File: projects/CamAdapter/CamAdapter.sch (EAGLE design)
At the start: 2 parts

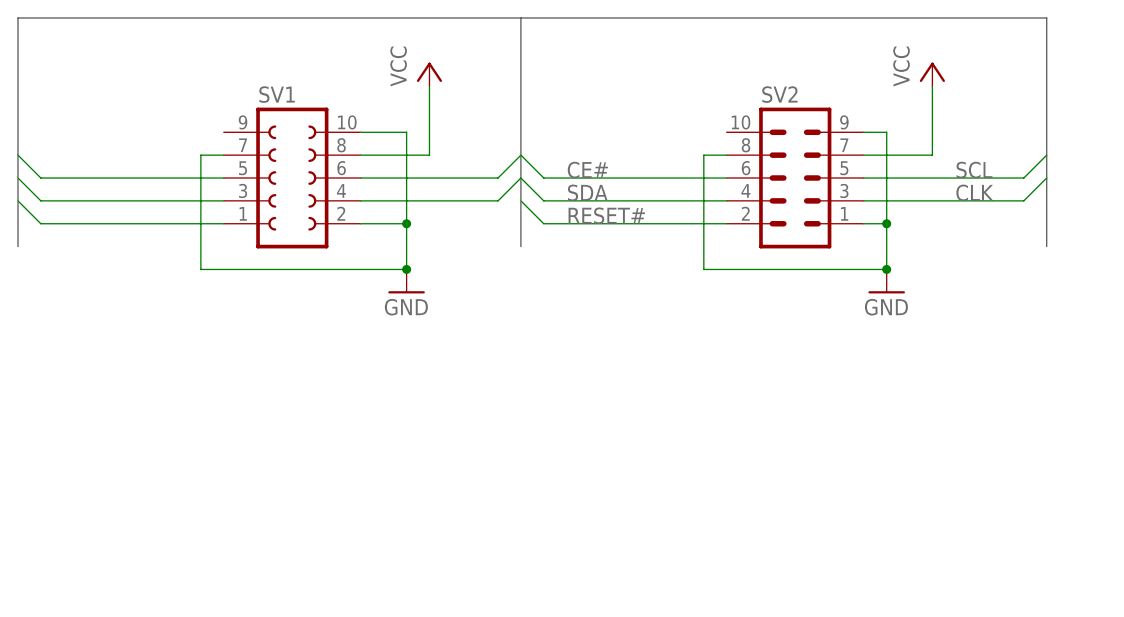
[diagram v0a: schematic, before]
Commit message: Updated CamAdapter + Board
* Added 25 MHz resonator to adapter board
* Removed 25 MHz CLK signal from PCB connector
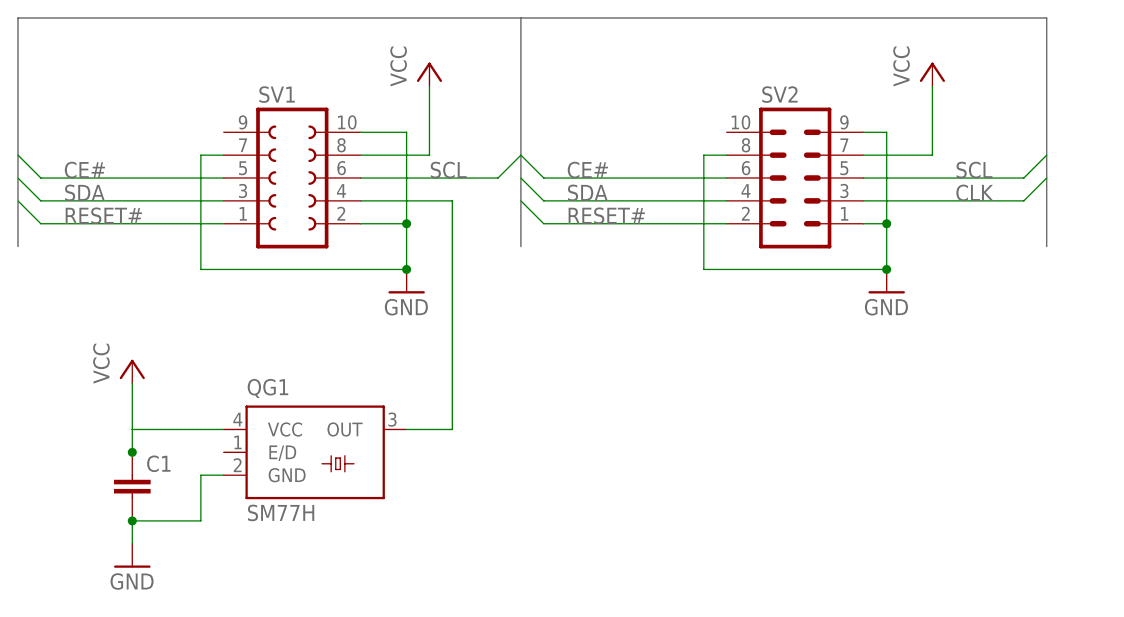
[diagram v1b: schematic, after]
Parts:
- added C1: (no value), resistor:C-EUC0805
- added QG1: SM77H, crystal:SM77H
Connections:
- new net N$1: QG1.OUT, SV1.4
- net CLK: no longer SV1.4
- net GND: now also C1.2, QG1.GND
- net VCC: now also C1.1, QG1.VCC
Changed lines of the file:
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@@
 <grid distance="0.1" unitdist="inch" unit="inch" style="lines" multiple="1" display="no" altdistance="0.01" altunitdist="inch" altunit="inch"/>
 <layers>
-<layer number="1" name="Top" color="4" fill="1" visible="no" active="no"/>
-<layer number="16" name="Bottom" color="1" fill="1" visible="no" active="no"/>
-<layer number="17" name="Pads" color="2" fill="1" visible="no" active="no"/>
-<layer number="18" name="Vias" color="2" fill="1" visible="no" active="no"/>
-<layer number="19" name="Unrouted" color="6" fill="1" visible="no" active="no"/>
-<layer number="20" name="Dimension" color="15" fill="1" visible="no" active="no"/>
-<layer number="21" name="tPlace" color="7" fill="1" visible="no" active="no"/>
-<layer number="22" name="bPlace" color="7" fill="1" visible="no" active="no"/>
-<layer number="23" name="tOrigins" color="15" fill="1" visible="no" active="no"/>
-<layer number="24" name="bOrigins" color="15" fill="1" visible="no" active="no"/>
-<layer number="25" name="tNames" color="7" fill="1" visible="no" active="no"/>
-<layer number="26" name="bNames" color="7" fill="1" visible="no" active="no"/>
-<layer number="27" name="tValues" color="7" fill="1" visible="no" active="no"/>
-<layer number="28" name="bValues" color="7" fill="1" visible="no" active="no"/>
+<layer number="1" name="Top" color="4" fill="1" visible="yes" active="no"/>
+<layer number="16" name="Bottom" color="1" fill="1" visible="yes" active="no"/>
+<layer number="17" name="Pads" color="2" fill="1" visible="yes" active="no"/>
+<layer number="18" name="Vias" color="2" fill="1" visible="yes" active="no"/>
+<layer number="19" name="Unrouted" color="6" fill="1" visible="yes" active="no"/>
+<layer number="20" name="Dimension" color="15" fill="1" visible="yes" active="no"/>
+<layer number="21" name="tPlace" color="7" fill="1" visible="yes" active="no"/>
+<layer number="22" name="bPlace" color="7" fill="1" visible="yes" active="no"/>
+<layer number="23" name="tOrigins" color="15" fill="1" visible="yes" active="no"/>
+<layer number="24" name="bOrigins" color="15" fill="1" visible="yes" active="no"/>
+<layer number="25" name="tNames" color="7" fill="1" visible="yes" active="no"/>
+<layer number="26" name="bNames" color="7" fill="1" visible="yes" active="no"/>
+<layer number="27" name="tValues" color="7" fill="1" visible="yes" active="no"/>
+<layer number="28" name="bValues" color="7" fill="1" visible="yes" active="no"/>
 <layer number="29" name="tStop" color="7" fill="3" visible="no" active="no"/>
 <layer number="30" name="bStop" color="7" fill="6" visible="no" active="no"/>
@@
 <layer number="35" name="tGlue" color="7" fill="4" visible="no" active="no"/>
 <layer number="36" name="bGlue" color="7" fill="5" visible="no" active="no"/>
-<layer number="37" name="tTest" color="7" fill="1" visible="no" active="no"/>
-<layer number="38" name="bTest" color="7" fill="1" visible="no" active="no"/>
+<layer number="37" name="tTest" color="7" fill="1" visible="yes" active="no"/>
+<layer number="38" name="bTest" color="7" fill="1" visible="yes" active="no"/>
 <layer number="39" name="tKeepout" color="4" fill="11" visible="no" active="no"/>
 <layer number="40" name="bKeepout" color="1" fill="11" visible="no" active="no"/>
@@
 <layer number="44" name="Drills" color="7" fill="1" visible="no" active="no"/>
 <layer number="45" name="Holes" color="7" fill="1" visible="no" active="no"/>
-<layer number="46" name="Milling" color="3" fill="1" visible="no" active="no"/>
-<layer number="47" name="Measures" color="7" fill="1" visible="no" active="no"/>
-<layer number="48" name="Document" color="7" fill="1" visible="no" active="no"/>
-<layer number="49" name="Reference" color="7" fill="1" visible="no" active="no"/>
-<layer number="51" name="tDocu" color="7" fill="1" visible="no" active="no"/>
-<layer number="52" name="bDocu" color="7" fill="1" visible="no" active="no"/>
+<layer number="46" name="Milling" color="3" fill="1" visible="yes" active="no"/>
+<layer number="47" name="Measures" color="7" fill="1" visible="yes" active="no"/>
+<layer number="48" name="Document" color="7" fill="1" visible="yes" active="no"/>
+<layer number="49" name="Reference" color="7" fill="1" visible="yes" active="no"/>
+<layer number="51" name="tDocu" color="7" fill="1" visible="yes" active="no"/>
+<layer number="52" name="bDocu" color="7" fill="1" visible="yes" active="no"/>
 <layer number="91" name="Nets" color="2" fill="1" visible="yes" active="yes"/>
 <layer number="92" name="Busses" color="1" fill="1" visible="yes" active="yes"/>
@@
 <part name="P+1" library="supply1" deviceset="VCC" device=""/>
 <part name="P+2" library="supply1" deviceset="VCC" device=""/>
+<part name="QG1" library="crystal" deviceset="SM77H" device=""/>
+<part name="C1" library="resistor" deviceset="C-EU" device="C0805"/>
+<part name="P+3" library="supply1" deviceset="VCC" device=""/>
+<part name="GND3" library="supply1" deviceset="GND" device=""/>
 </parts>
 <sheets>
@@
 <instance part="P+1" gate="VCC" x="93.98" y="127"/>
 <instance part="P+2" gate="VCC" x="149.86" y="127"/>
+<instance part="QG1" gate="G$1" x="81.28" y="83.82"/>
+<instance part="C1" gate="G$1" x="60.96" y="81.28"/>
+<instance part="P+3" gate="VCC" x="60.96" y="93.98"/>
+<instance part="GND3" gate="1" x="60.96" y="71.12"/>
 </instances>
 <busses>
@@
 <wire x1="71.12" y1="109.22" x2="50.8" y2="109.22" width="0.1524" layer="91"/>
 <wire x1="50.8" y1="109.22" x2="48.26" y2="111.76" width="0.1524" layer="91"/>
+<label x="53.34" y="109.22" size="1.778" layer="95"/>
 </segment>
 </net>
@@
 <label x="152.4" y="111.76" size="1.778" layer="95"/>
 </segment>
-<segment>
-<pinref part="SV1" gate="G$1" pin="4"/>
-<wire x1="86.36" y1="111.76" x2="101.6" y2="111.76" width="0.1524" layer="91"/>
-<wire x1="101.6" y1="111.76" x2="104.14" y2="114.3" width="0.1524" layer="91"/>
-</segment>
 </net>
 <net name="SDA" class="0">
@@
 <wire x1="71.12" y1="111.76" x2="50.8" y2="111.76" width="0.1524" layer="91"/>
 <wire x1="50.8" y1="111.76" x2="48.26" y2="114.3" width="0.1524" layer="91"/>
+<label x="53.34" y="111.76" size="1.778" layer="95"/>
 </segment>
 </net>
@@
 <wire x1="86.36" y1="114.3" x2="101.6" y2="114.3" width="0.1524" layer="91"/>
 <wire x1="101.6" y1="114.3" x2="104.14" y2="116.84" width="0.1524" layer="91"/>
+<label x="93.98" y="114.3" size="1.778" layer="95"/>
 </segment>
 </net>
@@
 <wire x1="71.12" y1="114.3" x2="50.8" y2="114.3" width="0.1524" layer="91"/>
 <wire x1="50.8" y1="114.3" x2="48.26" y2="116.84" width="0.1524" layer="91"/>
+<label x="53.34" y="114.3" size="1.778" layer="95"/>
 </segment>
 </net>
@@
 <junction x="91.44" y="109.22"/>
 </segment>
+<segment>
+<pinref part="QG1" gate="G$1" pin="GND"/>
+<wire x1="71.12" y1="81.28" x2="68.58" y2="81.28" width="0.1524" layer="91"/>
+<wire x1="68.58" y1="81.28" x2="68.58" y2="76.2" width="0.1524" layer="91"/>
+<pinref part="C1" gate="G$1" pin="2"/>
+<wire x1="68.58" y1="76.2" x2="60.96" y2="76.2" width="0.1524" layer="91"/>
+<pinref part="GND3" gate="1" pin="GND"/>
+<wire x1="60.96" y1="76.2" x2="60.96" y2="73.66" width="0.1524" layer="91"/>
+<junction x="60.96" y="76.2"/>
+</segment>
 </net>
 <net name="VCC" class="0">
@@
 <wire x1="93.98" y1="116.84" x2="93.98" y2="124.46" width="0.1524" layer="91"/>
 </segment>
-</net>
+<segment>
+<pinref part="QG1" gate="G$1" pin="VCC"/>
+<pinref part="P+3" gate="VCC" pin="VCC"/>
+<wire x1="71.12" y1="86.36" x2="60.96" y2="86.36" width="0.1524" layer="91"/>
+<wire x1="60.96" y1="86.36" x2="60.96" y2="91.44" width="0.1524" layer="91"/>
+<pinref part="C1" gate="G$1" pin="1"/>
+<wire x1="60.96" y1="83.82" x2="60.96" y2="86.36" width="0.1524" layer="91"/>
+<junction x="60.96" y="83.82"/>
+</segment>
+</net>
+<net name="N$1" class="0">
+<segment>
+<pinref part="QG1" gate="G$1" pin="OUT"/>
+<wire x1="91.44" y1="86.36" x2="96.52" y2="86.36" width="0.1524" layer="91"/>
+<wire x1="96.52" y1="86.36" x2="96.52" y2="111.76" width="0.1524" layer="91"/>
+<pinref part="SV1" gate="G$1" pin="4"/>
+<wire x1="96.52" y1="111.76" x2="86.36" y2="111.76" width="0.1524" layer="91"/>
+</segment>
+</net>

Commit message: Rev 2.0 RC
* TODO: Check CamAdapter.brd quarz oscillator package
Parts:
- C1: value (none) -> 100n
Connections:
- net VCC: now also QG1.E/D
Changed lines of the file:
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@@
 <part name="P+2" library="supply1" deviceset="VCC" device=""/>
 <part name="QG1" library="crystal" deviceset="SM77H" device=""/>
-<part name="C1" library="resistor" deviceset="C-EU" device="C0805"/>
+<part name="C1" library="resistor" deviceset="C-EU" device="C0805" value="100n"/>
 <part name="P+3" library="supply1" deviceset="VCC" device=""/>
 <part name="GND3" library="supply1" deviceset="GND" device=""/>
@@
 <wire x1="60.96" y1="83.82" x2="60.96" y2="86.36" width="0.1524" layer="91"/>
 <junction x="60.96" y="83.82"/>
+<pinref part="QG1" gate="G$1" pin="E/D"/>
+<wire x1="71.12" y1="83.82" x2="60.96" y2="83.82" width="0.1524" layer="91"/>
 </segment>
 </net>

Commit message: Enhaced space between signal trace and female pin header
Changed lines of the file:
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@@
 <grid distance="0.1" unitdist="inch" unit="inch" style="lines" multiple="1" display="no" altdistance="0.01" altunitdist="inch" altunit="inch"/>
 <layers>
-<layer number="1" name="Top" color="4" fill="1" visible="yes" active="no"/>
-<layer number="16" name="Bottom" color="1" fill="1" visible="yes" active="no"/>
-<layer number="17" name="Pads" color="2" fill="1" visible="yes" active="no"/>
-<layer number="18" name="Vias" color="2" fill="1" visible="yes" active="no"/>
-<layer number="19" name="Unrouted" color="6" fill="1" visible="yes" active="no"/>
-<layer number="20" name="Dimension" color="15" fill="1" visible="yes" active="no"/>
-<layer number="21" name="tPlace" color="7" fill="1" visible="yes" active="no"/>
-<layer number="22" name="bPlace" color="7" fill="1" visible="yes" active="no"/>
-<layer number="23" name="tOrigins" color="15" fill="1" visible="yes" active="no"/>
-<layer number="24" name="bOrigins" color="15" fill="1" visible="yes" active="no"/>
-<layer number="25" name="tNames" color="7" fill="1" visible="yes" active="no"/>
-<layer number="26" name="bNames" color="7" fill="1" visible="yes" active="no"/>
-<layer number="27" name="tValues" color="7" fill="1" visible="yes" active="no"/>
-<layer number="28" name="bValues" color="7" fill="1" visible="yes" active="no"/>
+<layer number="1" name="Top" color="4" fill="1" visible="no" active="no"/>
+<layer number="16" name="Bottom" color="1" fill="1" visible="no" active="no"/>
+<layer number="17" name="Pads" color="2" fill="1" visible="no" active="no"/>
+<layer number="18" name="Vias" color="2" fill="1" visible="no" active="no"/>
+<layer number="19" name="Unrouted" color="6" fill="1" visible="no" active="no"/>
+<layer number="20" name="Dimension" color="15" fill="1" visible="no" active="no"/>
+<layer number="21" name="tPlace" color="7" fill="1" visible="no" active="no"/>
+<layer number="22" name="bPlace" color="7" fill="1" visible="no" active="no"/>
+<layer number="23" name="tOrigins" color="15" fill="1" visible="no" active="no"/>
+<layer number="24" name="bOrigins" color="15" fill="1" visible="no" active="no"/>
+<layer number="25" name="tNames" color="7" fill="1" visible="no" active="no"/>
+<layer number="26" name="bNames" color="7" fill="1" visible="no" active="no"/>
+<layer number="27" name="tValues" color="7" fill="1" visible="no" active="no"/>
+<layer number="28" name="bValues" color="7" fill="1" visible="no" active="no"/>
 <layer number="29" name="tStop" color="7" fill="3" visible="no" active="no"/>
 <layer number="30" name="bStop" color="7" fill="6" visible="no" active="no"/>
@@
 <layer number="35" name="tGlue" color="7" fill="4" visible="no" active="no"/>
 <layer number="36" name="bGlue" color="7" fill="5" visible="no" active="no"/>
-<layer number="37" name="tTest" color="7" fill="1" visible="yes" active="no"/>
-<layer number="38" name="bTest" color="7" fill="1" visible="yes" active="no"/>
+<layer number="37" name="tTest" color="7" fill="1" visible="no" active="no"/>
+<layer number="38" name="bTest" color="7" fill="1" visible="no" active="no"/>
 <layer number="39" name="tKeepout" color="4" fill="11" visible="no" active="no"/>
 <layer number="40" name="bKeepout" color="1" fill="11" visible="no" active="no"/>
@@
 <layer number="44" name="Drills" color="7" fill="1" visible="no" active="no"/>
 <layer number="45" name="Holes" color="7" fill="1" visible="no" active="no"/>
-<layer number="46" name="Milling" color="3" fill="1" visible="yes" active="no"/>
-<layer number="47" name="Measures" color="7" fill="1" visible="yes" active="no"/>
-<layer number="48" name="Document" color="7" fill="1" visible="yes" active="no"/>
-<layer number="49" name="Reference" color="7" fill="1" visible="yes" active="no"/>
-<layer number="51" name="tDocu" color="7" fill="1" visible="yes" active="no"/>
-<layer number="52" name="bDocu" color="7" fill="1" visible="yes" active="no"/>
+<layer number="46" name="Milling" color="3" fill="1" visible="no" active="no"/>
+<layer number="47" name="Measures" color="7" fill="1" visible="no" active="no"/>
+<layer number="48" name="Document" color="7" fill="1" visible="no" active="no"/>
+<layer number="49" name="Reference" color="7" fill="1" visible="no" active="no"/>
+<layer number="51" name="tDocu" color="7" fill="1" visible="no" active="no"/>
+<layer number="52" name="bDocu" color="7" fill="1" visible="no" active="no"/>
 <layer number="91" name="Nets" color="2" fill="1" visible="yes" active="yes"/>
 <layer number="92" name="Busses" color="1" fill="1" visible="yes" active="yes"/>
@@
 <pinref part="QG1" gate="G$1" pin="E/D"/>
 <wire x1="71.12" y1="83.82" x2="60.96" y2="83.82" width="0.1524" layer="91"/>
+<junction x="60.96" y="86.36"/>
 </segment>
 </net>
@@
 </sheet>
 </sheets>
+<errors>
+</errors>
 </schematic>
 </drawing>

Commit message: pcb2gcode outline & drill test
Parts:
- added JP1: (no value), pinhead:PINHD-1X3
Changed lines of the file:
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@@
 <part name="P+3" library="supply1" deviceset="VCC" device=""/>
 <part name="GND3" library="supply1" deviceset="GND" device=""/>
+<part name="JP1" library="pinhead" deviceset="PINHD-1X3" device=""/>
 </parts>
 <sheets>
@@
 <instance part="P+3" gate="VCC" x="60.96" y="93.98"/>
 <instance part="GND3" gate="1" x="60.96" y="71.12"/>
+<instance part="JP1" gate="A" x="167.64" y="91.44"/>
 </instances>
 <busses>

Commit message: Final
* finally found out pcb2gcode and CAM settings so that
  lower right corner is origin and coordinates relative to that point
	lign up when CNC milling
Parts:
- removed JP1: (no value), pinhead:PINHD-1X3
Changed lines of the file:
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@@
 <part name="P+3" library="supply1" deviceset="VCC" device=""/>
 <part name="GND3" library="supply1" deviceset="GND" device=""/>
-<part name="JP1" library="pinhead" deviceset="PINHD-1X3" device=""/>
 </parts>
 <sheets>
@@
 <instance part="P+3" gate="VCC" x="60.96" y="93.98"/>
 <instance part="GND3" gate="1" x="60.96" y="71.12"/>
-<instance part="JP1" gate="A" x="167.64" y="91.44"/>
 </instances>
 <busses>
